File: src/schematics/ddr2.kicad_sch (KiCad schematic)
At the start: 23 parts, among them U11 IS43DR86400E

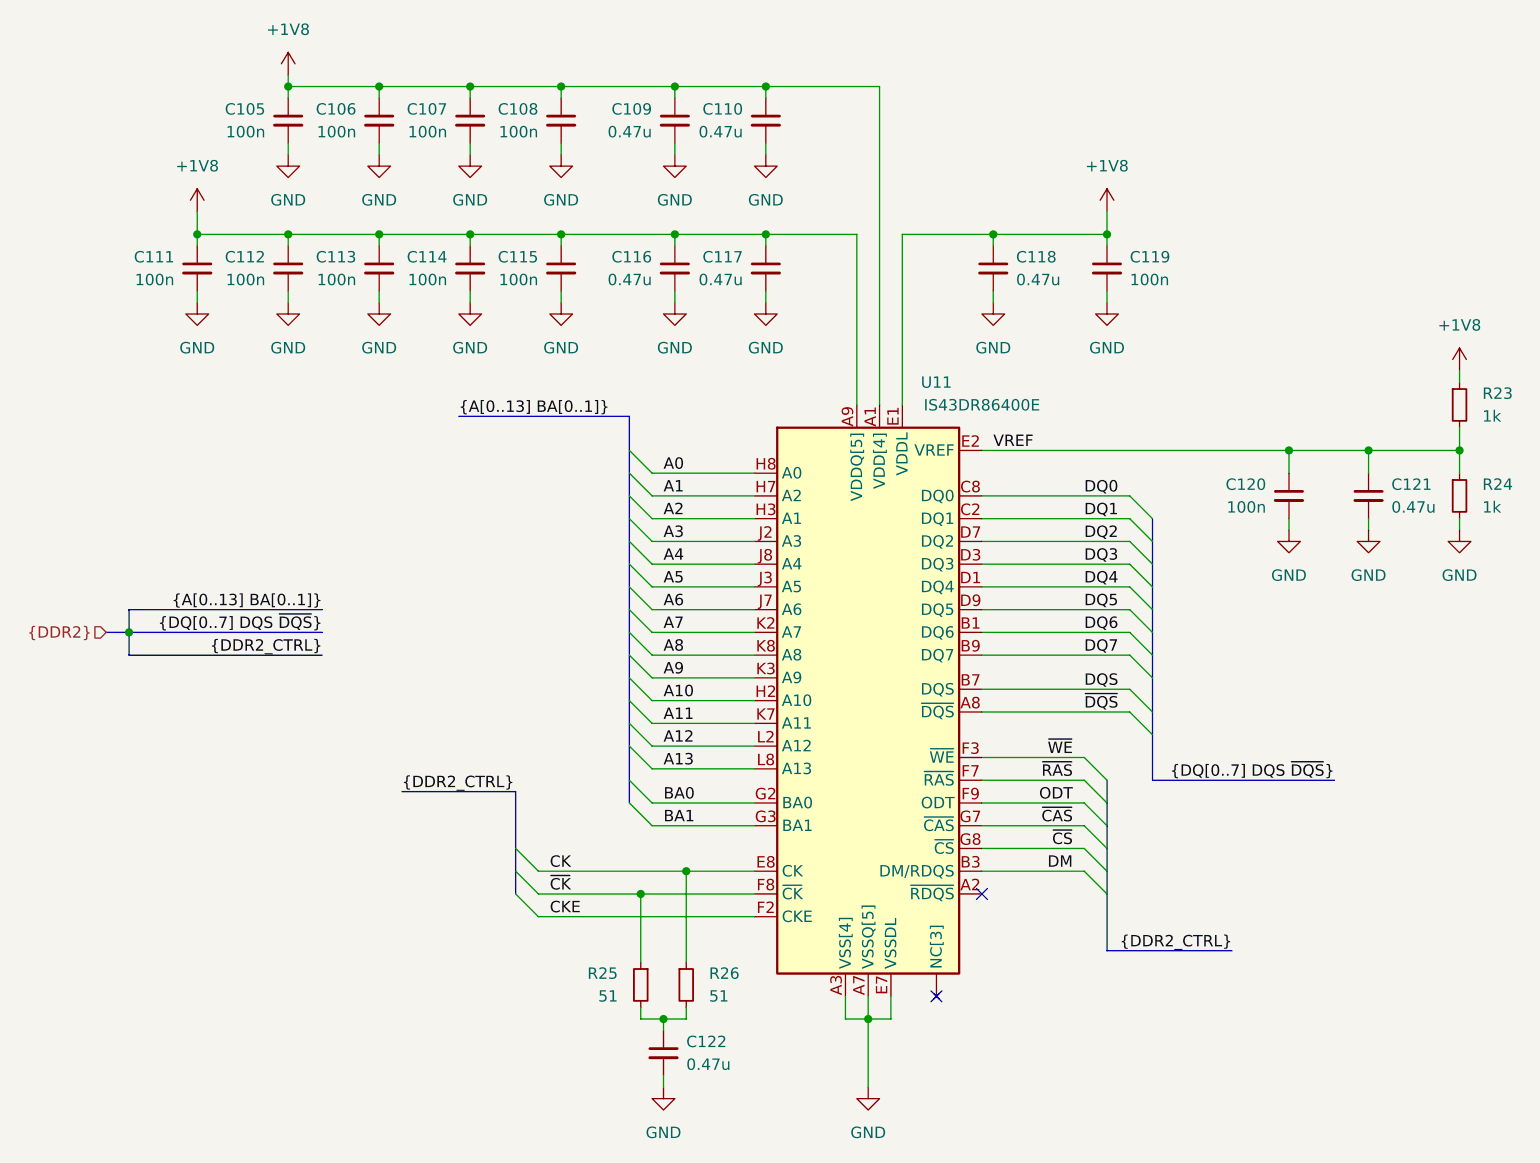
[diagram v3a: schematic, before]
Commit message: Fixes bus aliases
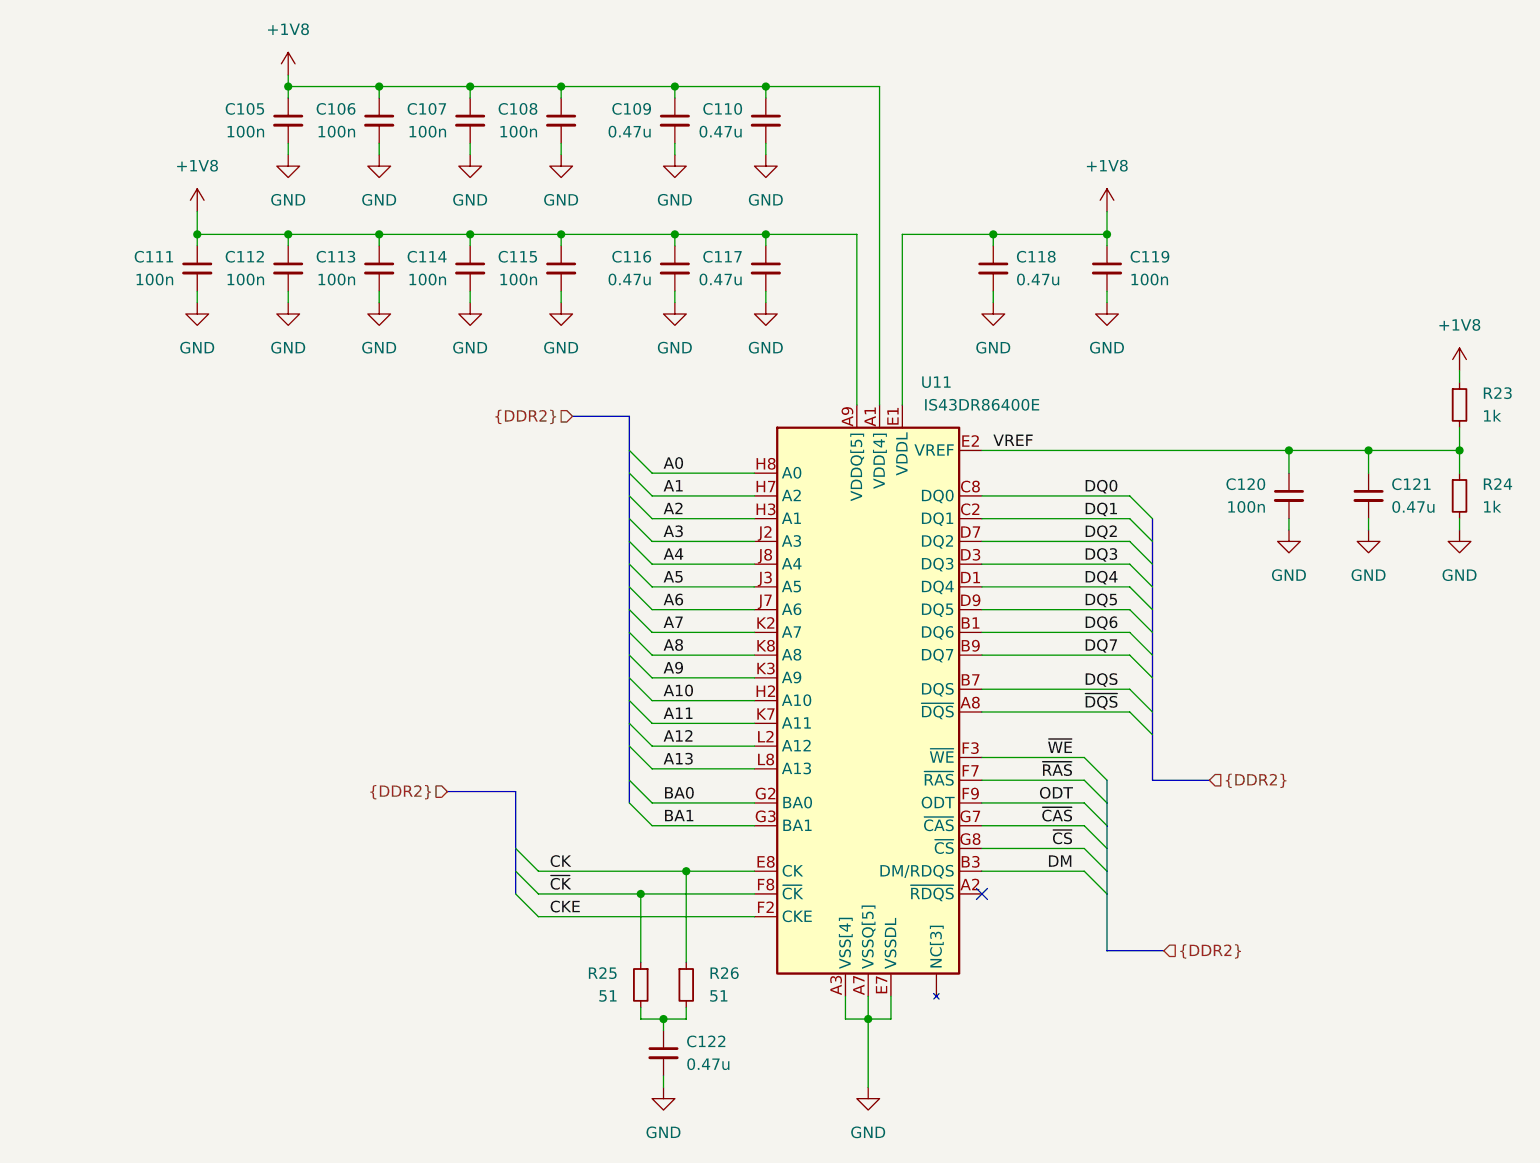
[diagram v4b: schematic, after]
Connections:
- no-connect marks 2 -> 1
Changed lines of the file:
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@@
 	)
 	(bus_alias "DDR2"
-		(members "A[0..13]" "BA[0..1]" "DQ[0..7]" "DQS" "~{DQS}" "{DDR2_CTRL}")
-	)
-	(bus_alias "DDR2_CTRL"
-		(members "~{LB}" "~{UB}" "~{WE}" "~{OE}" "~{CE}")
+		(members "A[0..13]" "BA[0..1]" "DQ[0..7]" "DQS" "~{DQS}" "CK" "~{CK}" "CKE"
+			"~{WE}" "~{RAS}" "ODT" "~{CAS}" "~{CS}" "DM"
+		)
 	)
 	(junction
@@
 	)
 	(junction
-		(at 67.31 92.71)
-		(diameter 0)
-		(color 0 0 0 0)
-	)
-	(junction
 		(at 129.54 119.38)
 		(diameter 0)
@@
 	)
 	(no_connect
-		(at 157.48 133.35)
-	)
-	(no_connect
 		(at 162.56 121.92)
 	)
@@
 	(bus
 		(pts
-			(xy 104.14 68.58) (xy 123.19 68.58)
+			(xy 116.84 68.58) (xy 123.19 68.58)
 		)
 		(stroke
@@
 		)
 	)
-	(bus
-		(pts
-			(xy 67.31 92.71) (xy 88.9 92.71)
-		)
-		(stroke
-			(width 0)
-			(type default)
-		)
-	)
 	(wire
 		(pts
@@
 	(bus
 		(pts
-			(xy 97.79 110.49) (xy 110.49 110.49)
+			(xy 102.87 110.49) (xy 110.49 110.49)
 		)
 		(stroke
@@
 	(bus
 		(pts
-			(xy 67.31 92.71) (xy 67.31 95.25)
-		)
-		(stroke
-			(width 0)
-			(type default)
-		)
-	)
-	(bus
-		(pts
 			(xy 123.19 105.41) (xy 123.19 102.87)
 		)
@@
 		)
 	)
-	(bus
-		(pts
-			(xy 67.31 92.71) (xy 67.31 90.17)
-		)
-		(stroke
-			(width 0)
-			(type default)
-		)
-	)
 	(wire
 		(pts
@@
 	(bus
 		(pts
-			(xy 176.53 128.27) (xy 190.5 128.27)
+			(xy 176.53 128.27) (xy 182.88 128.27)
 		)
 		(stroke
@@
 		)
 	)
-	(bus
-		(pts
-			(xy 64.77 92.71) (xy 67.31 92.71)
-		)
-		(stroke
-			(width 0)
-			(type default)
-		)
-	)
 	(wire
 		(pts
@@
 		)
 	)
-	(bus
-		(pts
-			(xy 67.31 90.17) (xy 88.9 90.17)
-		)
-		(stroke
-			(width 0)
-			(type default)
-		)
-	)
 	(wire
 		(pts
@@
 	(bus
 		(pts
-			(xy 181.61 109.22) (xy 201.93 109.22)
+			(xy 181.61 109.22) (xy 187.96 109.22)
 		)
 		(stroke
@@
 	(bus
 		(pts
-			(xy 88.9 95.25) (xy 67.31 95.25)
-		)
-		(stroke
-			(width 0)
-			(type default)
-		)
-	)
-	(bus
-		(pts
 			(xy 181.61 82.55) (xy 181.61 80.01)
 		)
@@
 			(width 0)
 			(type default)
-		)
-	)
-	(label "{DDR2_CTRL}"
-		(at 88.9 95.25 180)
-		(fields_autoplaced yes)
-		(effects
-			(font
-				(size 1.27 1.27)
-			)
-			(justify right bottom)
 		)
 	)
@@
 		)
 	)
-	(label "{A[0..13] BA[0..1]}"
-		(at 88.9 90.17 180)
-		(fields_autoplaced yes)
-		(effects
-			(font
-				(size 1.27 1.27)
-			)
-			(justify right bottom)
-		)
-	)
 	(label "DQS"
 		(at 177.8 99.06 180)
@@
 		)
 	)
-	(label "{DDR2_CTRL}"
-		(at 190.5 128.27 180)
-		(fields_autoplaced yes)
-		(effects
-			(font
-				(size 1.27 1.27)
-			)
-			(justify right bottom)
-		)
-	)
 	(label "DM"
 		(at 172.72 119.38 180)
@@
 		)
 	)
-	(label "{DQ[0..7] DQS ~{DQS}}"
-		(at 88.9 92.71 180)
-		(fields_autoplaced yes)
-		(effects
-			(font
-				(size 1.27 1.27)
-			)
-			(justify right bottom)
-		)
-	)
 	(label "A0"
 		(at 127 74.93 0)
@@
 		)
 	)
-	(label "{DQ[0..7] DQS ~{DQS}}"
-		(at 201.93 109.22 180)
-		(fields_autoplaced yes)
-		(effects
-			(font
-				(size 1.27 1.27)
-			)
-			(justify right bottom)
-		)
-	)
 	(label "ODT"
 		(at 172.72 111.76 180)
@@
 		)
 	)
-	(label "{DDR2_CTRL}"
-		(at 97.79 110.49 0)
-		(fields_autoplaced yes)
-		(effects
-			(font
-				(size 1.27 1.27)
-			)
-			(justify left bottom)
-		)
-	)
-	(label "{A[0..13] BA[0..1]}"
-		(at 104.14 68.58 0)
-		(fields_autoplaced yes)
-		(effects
-			(font
-				(size 1.27 1.27)
-			)
-			(justify left bottom)
-		)
-	)
 	(label "A1"
 		(at 127 77.47 0)
@@
 	(hierarchical_label "{DDR2}"
 		(shape input)
-		(at 64.77 92.71 180)
-		(fields_autoplaced yes)
-		(effects
+		(at 102.87 110.49 180)
+		(fields_autoplaced yes)
+		(effects
+			(font
+				(size 1.27 1.27)
+			)
+			(justify right)
+		)
+	)
+	(hierarchical_label "{DDR2}"
+		(shape input)
+		(at 182.88 128.27 0)
+		(fields_autoplaced yes)
+		(effects
+			(font
+				(size 1.27 1.27)
+			)
+			(justify left)
+		)
+	)
+	(hierarchical_label "{DDR2}"
+		(shape input)
+		(at 187.96 109.22 0)
+		(fields_autoplaced yes)
+		(effects
+			(font
+				(size 1.27 1.27)
+			)
+			(justify left)
+		)
+	)
+	(hierarchical_label "{DDR2}"
+		(shape input)
+		(at 116.84 68.58 180)
+		(fields_autoplaced yes)
+		(effects

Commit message: Remove bus groups
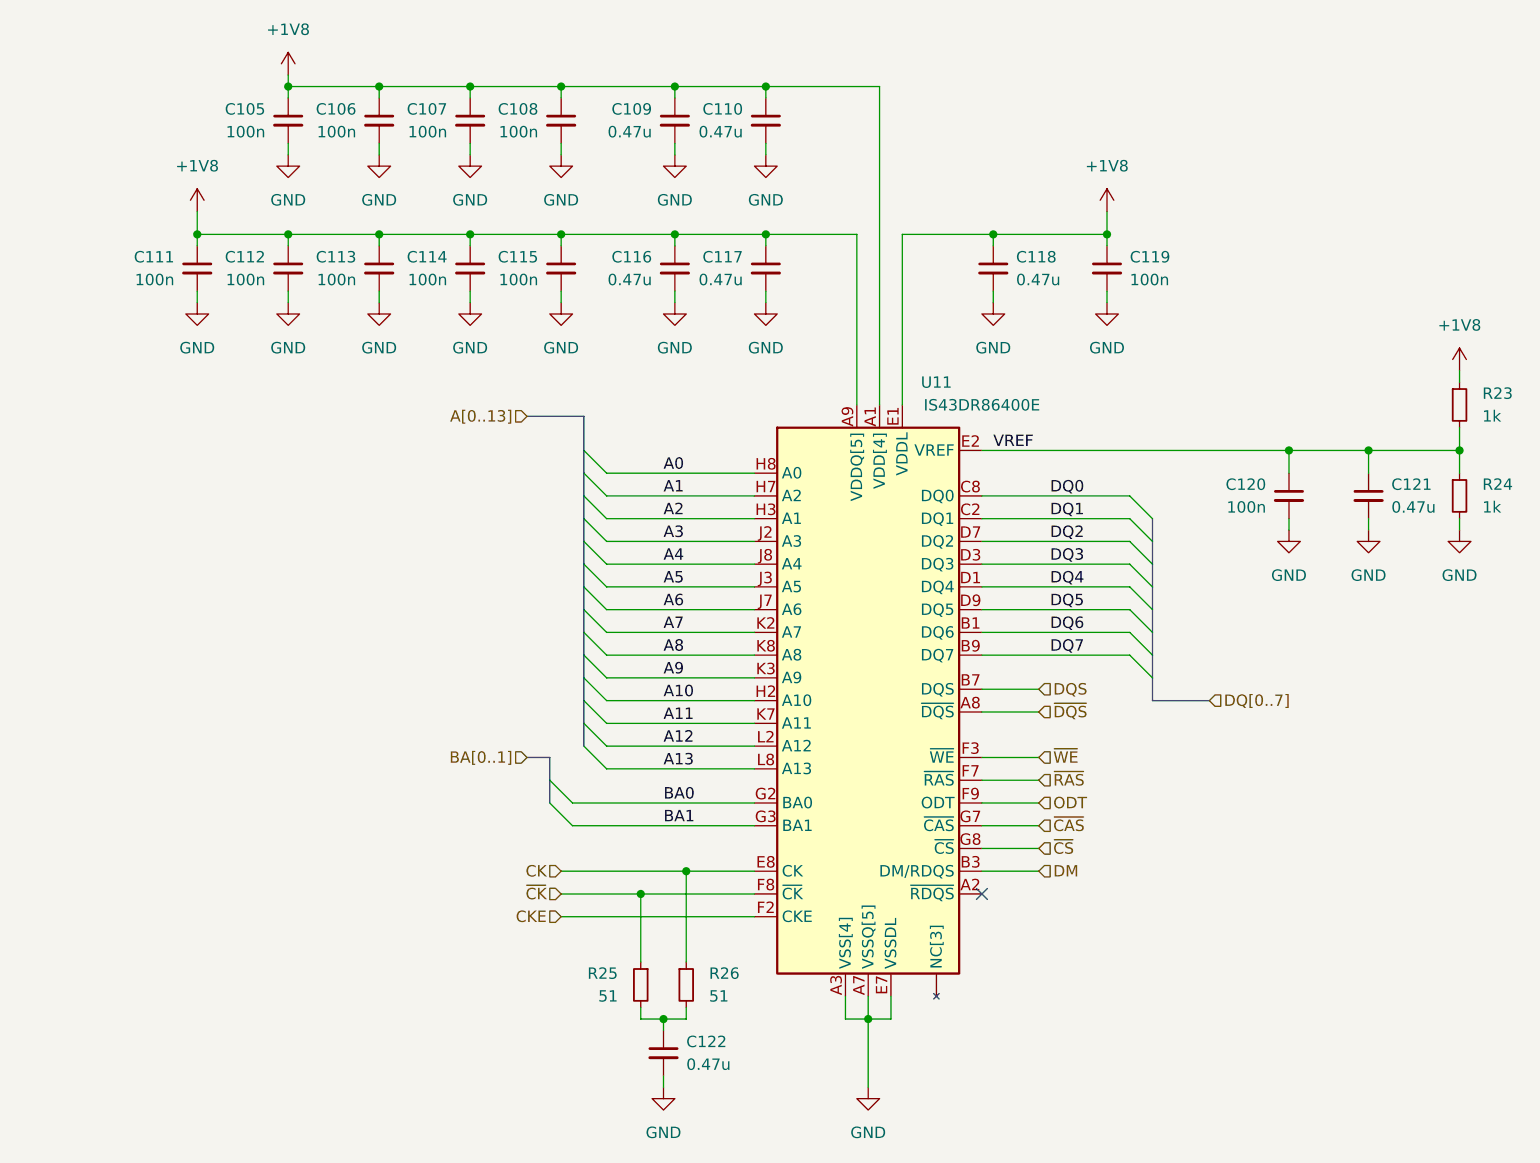
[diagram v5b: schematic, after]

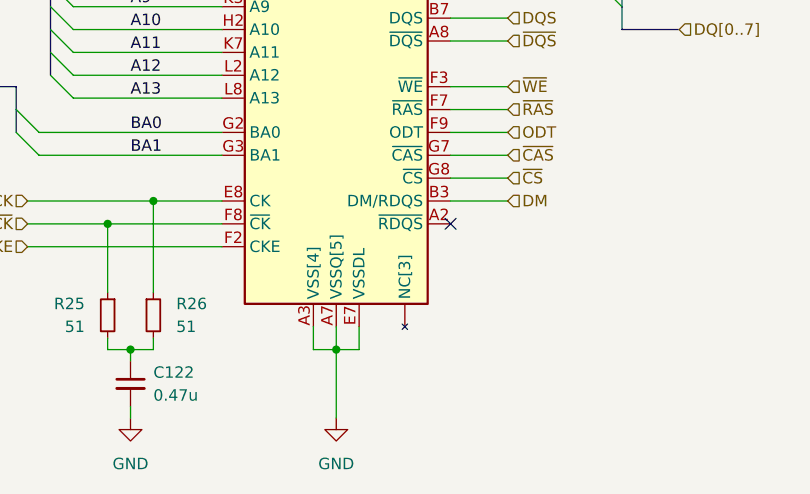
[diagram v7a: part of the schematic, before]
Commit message: ✅ Validate the DDR2 symbols
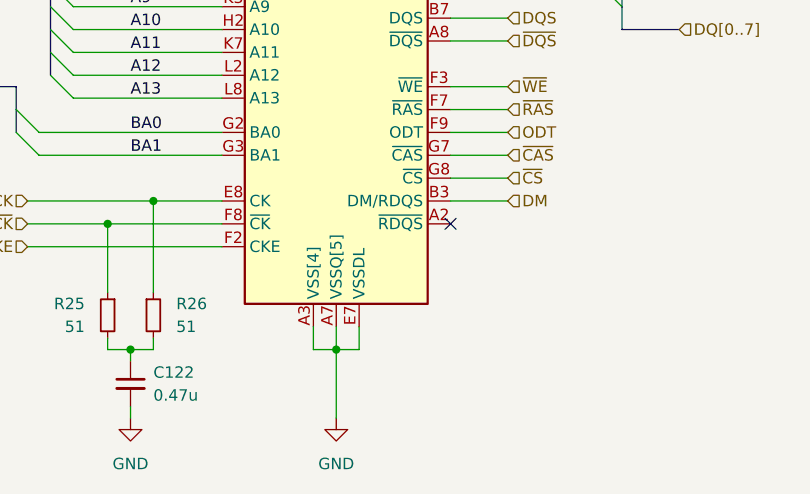
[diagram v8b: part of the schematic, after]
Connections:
- net at U11.G1 (NC[3]), U11.L3 (NC), U11.L7 (NC): no longer U11. (NC[3])
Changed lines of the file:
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@@
 			)
 		)
-		(property "Description" "32Mx16 DDR2 DRAM"
+		(property "Description" "64Mx8 DDR2 DRAM"
 			(at 141.986 147.32 0)
 			(effects
@@
 		(pin "A1"
 		)
-		(pin ""
-		)
 		(pin "A2"
